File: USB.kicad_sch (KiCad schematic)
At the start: 84 parts, among them J1 PinHeader_1x3_P2.54mm_Drill1.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, J15 USB-C_Amphenol_12401598E4, J16 USB-C_Amphenol_12401598E4, J2 USB-C_Amphenol_12401598E4, U1 USB7252C, U2 HD3SS3220IRNHR, U3 TPD4E05U06QDQARQ1, U4 TPD4E05U06QDQARQ1, U46 AP7366_SOT, U47 TPD4E05U06QDQARQ1, U48 W25Q80DV_USON, U49 TPD4E05U06QDQARQ1, U50 TPD4E05U06QDQARQ1, U51 TPD4E05U06QDQARQ1, Y3 Oscillator_25MHz_ESC_2016MV

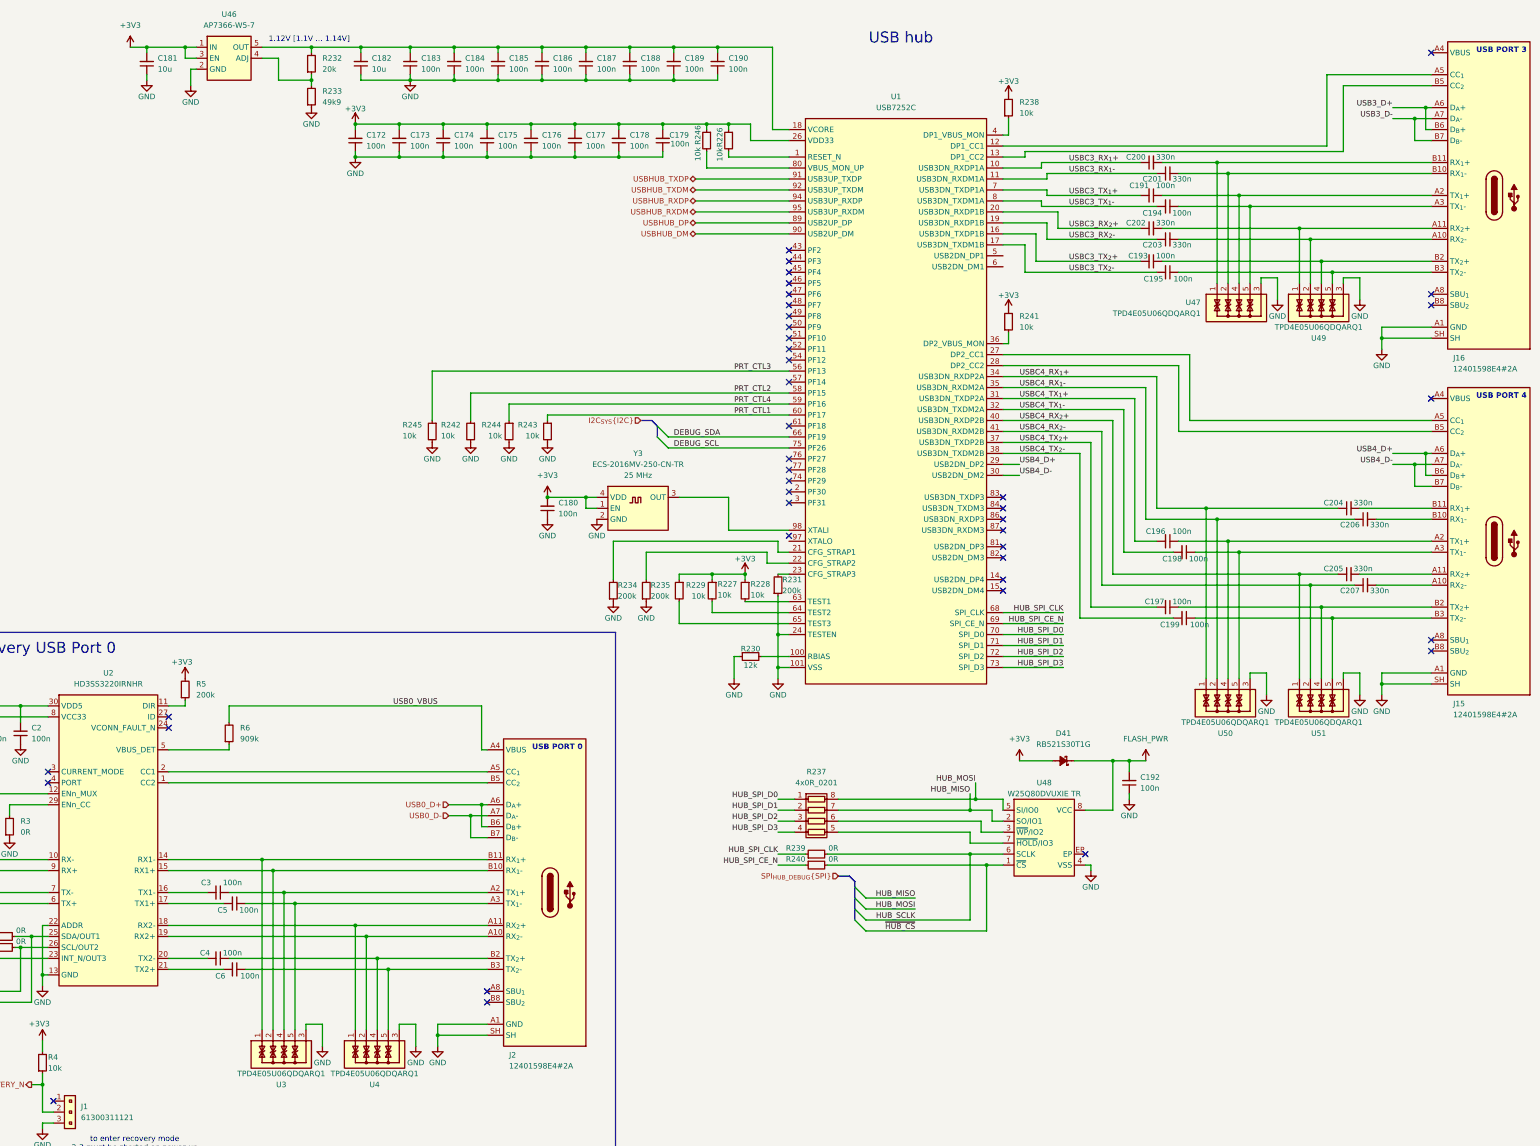
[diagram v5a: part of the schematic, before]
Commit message: [#82055] Fix labels
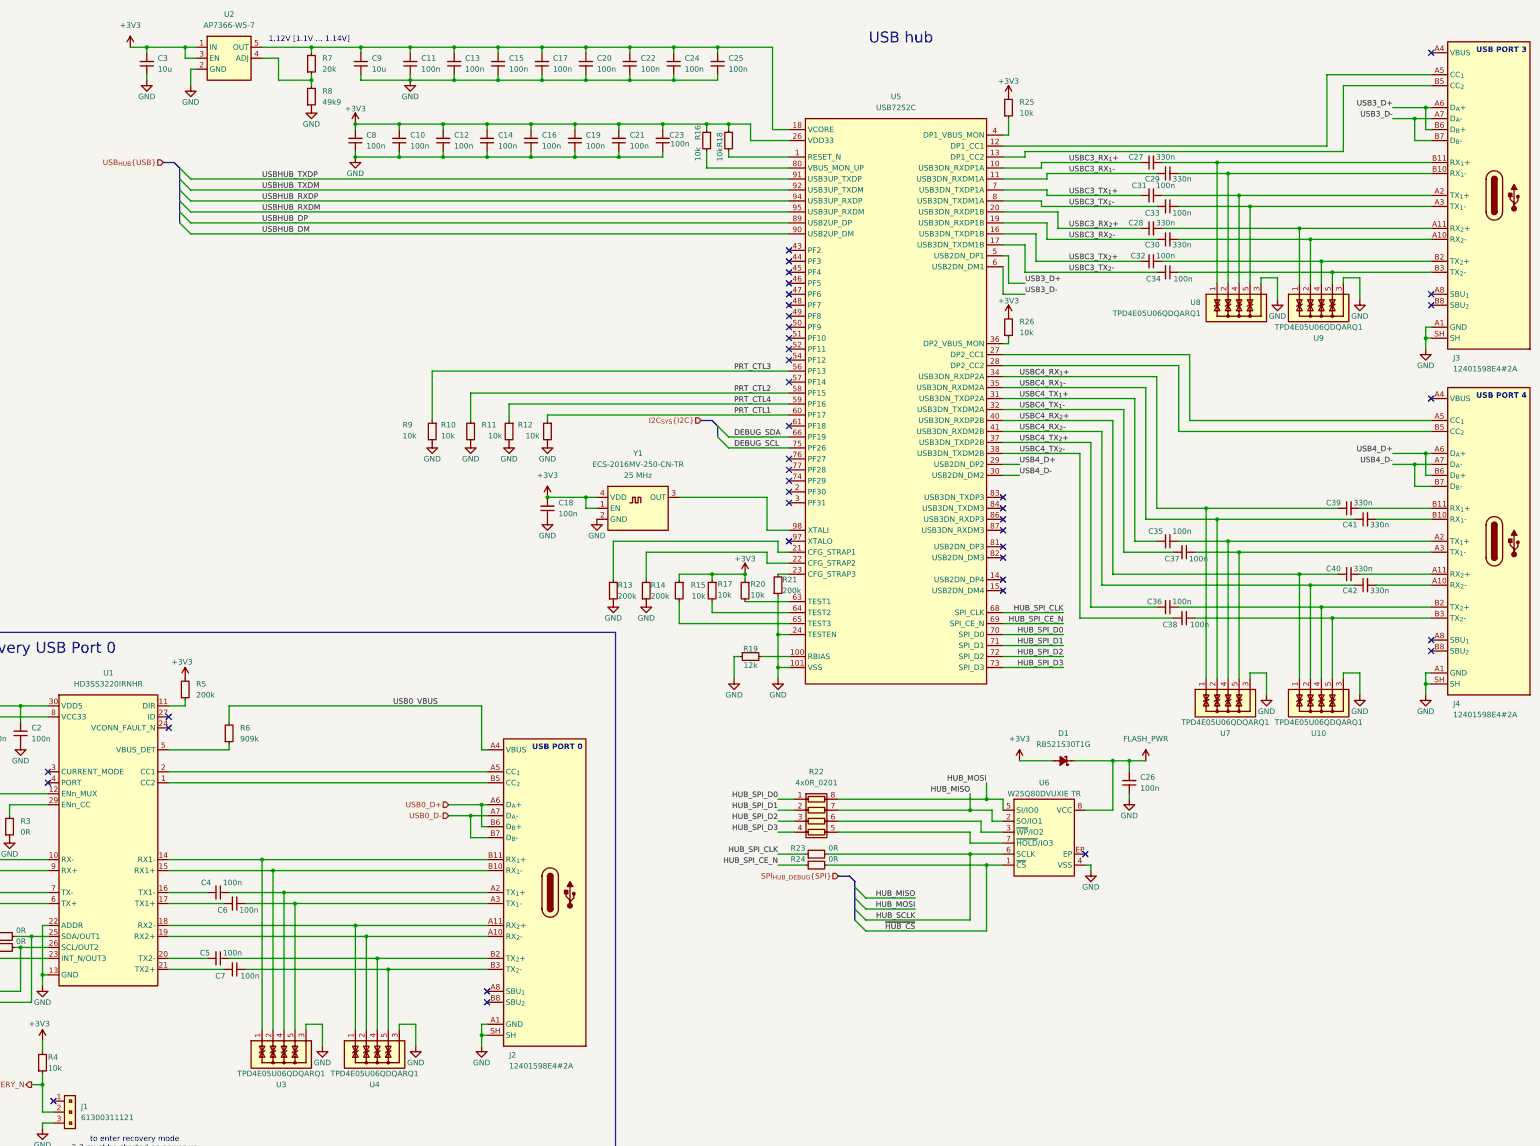
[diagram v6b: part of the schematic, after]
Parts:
- renumbered C173 to C10, C183 to C11, C174 to C12, C184 to C13, C175 to C14, C185 to C15, C176 to C16, C186 to C17, C180 to C18, C177 to C19, C187 to C20, C178 to C21, C188 to C22, C179 to C23, C189 to C24, C190 to C25, C192 to C26, C200 to C27, C202 to C28, C201 to C29, C181 to C3, C203 to C30, C191 to C31, C193 to C32, C194 to C33, C195 to C34, C196 to C35, C197 to C36, C198 to C37, C199 to C38, C204 to C39, C3 to C4, C205 to C40, C206 to C41, C207 to C42, C4 to C5, C5 to C6, C6 to C7, C172 to C8, C182 to C9, D41 to D1, J16 to J3, J15 to J4, R242 to R10, R244 to R11, R243 to R12, R234 to R13, R235 to R14, R229 to R15, R246 to R16, R227 to R17, R226 to R18, R230 to R19, R228 to R20, R231 to R21, R237 to R22, R239 to R23, R240 to R24, R238 to R25, R241 to R26, R232 to R7, R233 to R8, R245 to R9, U2 to U1, U51 to U10, U46 to U2, U1 to U5, U48 to U6, U50 to U7, U47 to U8, U49 to U9, Y3 to Y1
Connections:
- net USB3_D+: now also U5.5 (USB2DN_DP1)
- net USB3_D-: now also U5.6 (USB2DN_DM1)
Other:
- moved on the sheet: R26

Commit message: [#82055] Add ESD protection
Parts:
- added U52, U53, U54: TPD4E05U06QDQARQ1, antmicro-footprints:USON-10_2.5x1mm_P0.5mm, symbol antmicroTVSDiodes:TPD4E05U06QDQARQ1
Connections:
- net GND: now also U52.3, U52.8, U53.3, U53.8, U54.3, U54.8
- net USB0_VBUS: now also U52.5, U52.6
- net USB3_D+: now also U54.2, U54.9
- net USB3_D-: now also U54.1, U54.10
- net USB4_D+: now also U53.2, U53.9
- net USB4_D-: now also U53.1, U53.10
- net at J3.A5 (CC_{1}), U5.12 (DP1_CC1): now also U54.5, U54.6
- net at J3.B5 (CC_{2}), U5.13 (DP1_CC2): now also U54.4, U54.7
- net at J4.A5 (CC_{1}), U5.27 (DP2_CC1): now also U53.5, U53.6
- net at J4.B5 (CC_{2}), U5.28 (DP2_CC2): now also U53.4, U53.7
- net at J2.B5 (CC_{2}), U1.1 (CC2): now also U52.2, U52.9
- net at J2.A5 (CC_{1}), U1.2 (CC1): now also U52.4, U52.7
- new net: U52.1, U52.10
- no-connect marks 41 -> 42
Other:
- note added: "USB Hub flash"
- moved on the sheet: C10, C11, C12, C13, C14, C15, C16, C17, C19, C20, C21, C22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

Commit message: [#82055] Update USB hub symbol
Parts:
- U5: MPN USB7252C -> USB7252CT-I/KDX; Manufacturer Microchip -> Microchip Technology
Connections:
- net DEBUG_SCL: now also U5.66 (PF19); no longer U5.75 (PF26)
- net DEBUG_SDA: now also U5.61 (PF18); no longer U5.66 (PF19)
- net GND: no longer C11.1, C13.1, C15.1, C17.1, C20.1, C22.1, C24.1, C25.1
- net PRT_CTL1: now also U5.59 (PF16); no longer U5.60 (PF17)
- net PRT_CTL2: now also U5.57 (PF14); no longer U5.58 (PF15)
- net PRT_CTL3: now also U5.54 (PF12); no longer U5.56 (PF13)
- net PRT_CTL4: now also U5.58 (PF15); no longer U5.59 (PF16)
- net USBC3_RX_{2}+: now also U5.19 (USB3DN_RXDP1B); no longer U5.20 (USB3DN_RXDP1B)
- net USBC3_RX_{2}-: now also U5.20 (USB3DN_RXDM1B); no longer U5.19 (USB3DN_RXDP1B)
- net +1V12: now reaches C11.2, C13.2, C15.2, C17.2, C20.2, C22.2, C24.2, C25.2, C9.2, R7.2, U2.5 (OUT), U5.18 (VCORE), U5.25 (VCORE), U5.33 (VCORE), U5.39 (VCORE), U5.55 (VCORE), U5.78 (VCORE), U5.85 (VCORE), U5.9 (VCORE), U5.93 (VCORE)
- net +1V12: now also C11.1, C13.1, C15.1, C17.1, C20.1, C22.1, C24.1, C25.1
- net USB4_CC_{1}: now reaches J4.A5 (CC_{1}), U5.27 (DP2_CC1), U53.5, U53.6
- net USB4_CC_{2}: now reaches J4.B5 (CC_{2}), U5.28 (DP2_CC2), U53.4, U53.7
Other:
- note added: "USB hub LDO"
- moved on the sheet: C1, C2, C27, C28, C29, C3, C30, C31, C32, C33, C34, C4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
